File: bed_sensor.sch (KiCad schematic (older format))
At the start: 22 parts, among them J1 Conn_01x02, J4 Conn_01x02, J5 DM3AT-SF-PEJM5, Q1 2N2219, SW1 SW_SPST, U1 MIC5205-3.3, U2 MPU-9250, U5 CFAH0802D-YYH-JP

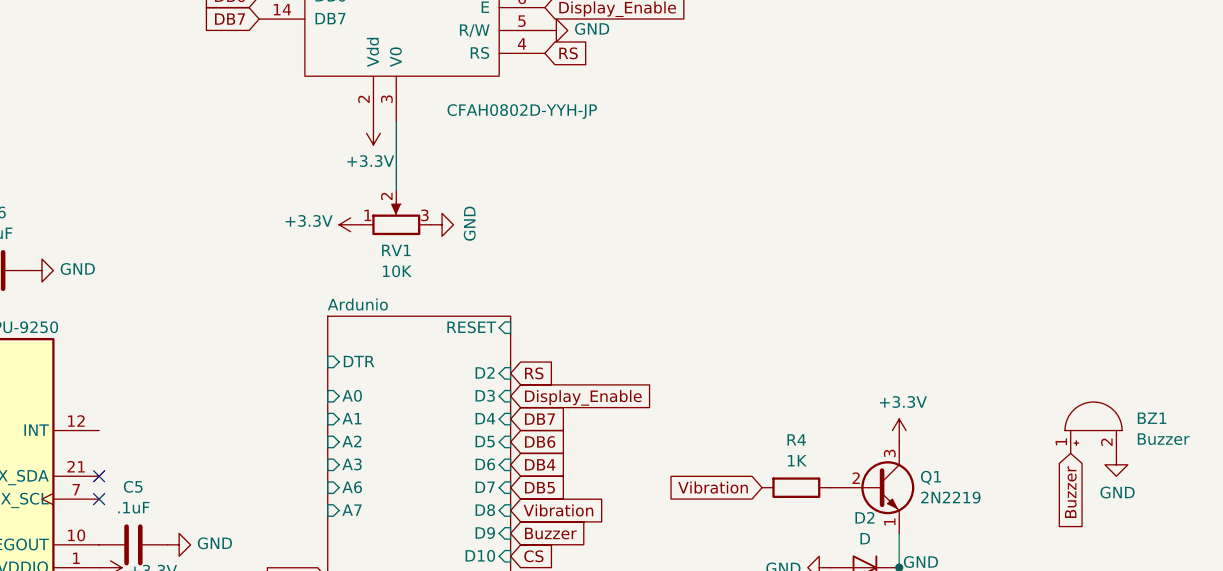
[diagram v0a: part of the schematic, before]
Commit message: added toggle button to side of board
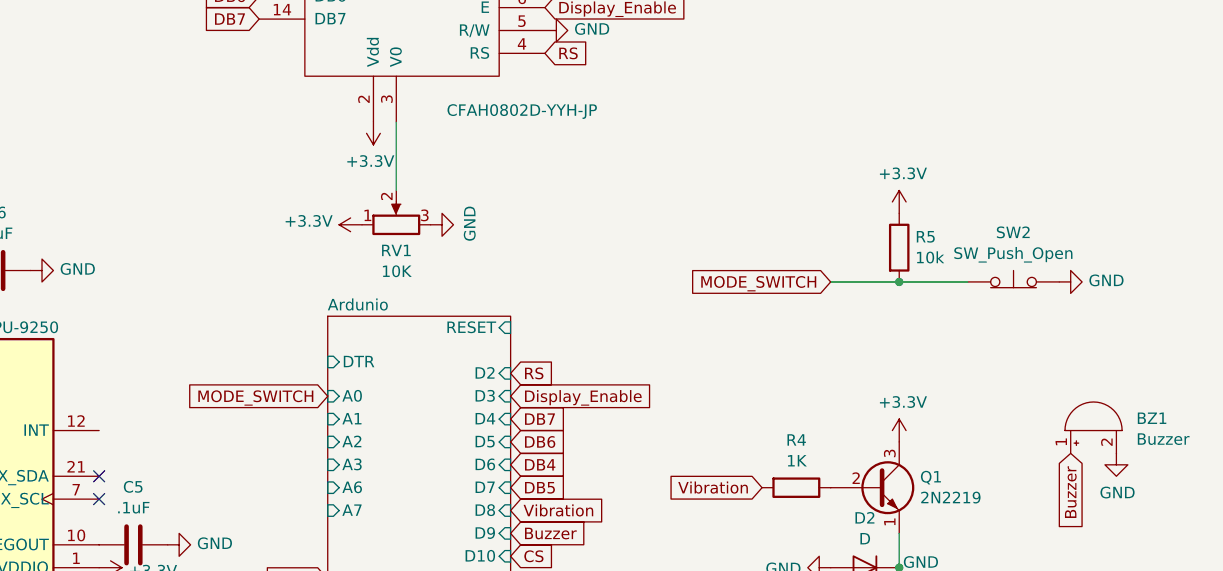
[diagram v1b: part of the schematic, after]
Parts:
- added R5: 10k, Resistor_SMD:R_0805_2012Metric, symbol Device:R
- added SW2: SW_Push_Open, Button_Switch_THT:SW_Tactile_SKHH_Angled, symbol Switch:SW_Push_Open
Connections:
- net +3V3: now also R5.1
- net GND: now also SW2.2 (B)
- new net MODE_SWITCH: R5.2, SW2.1 (A)
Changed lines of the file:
@@
 SCK
 $Comp
-L power:GND #PWR?
+L power:GND #PWR0117
 U 1 1 5B293C50
 P 4350 7200
-F 0 "#PWR?" H 4350 6950 50  0001 C CNN
+F 0 "#PWR0117" H 4350 6950 50  0001 C CNN
 F 1 "GND" V 4355 7072 50  0000 R CNN
 F 2 "" H 4350 7200 50  0001 C CNN
@@
 Text GLabel 4350 6600 0    50   Input ~ 0
 MISO
+$Comp
+L power:+3.3V #PWR0120
+U 1 1 5B2D3738
+P 7050 3800
+F 0 "#PWR0120" H 7050 3650 50  0001 C CNN
+F 1 "+3.3V" H 7065 3973 50  0000 C CNN
+F 2 "" H 7050 3800 50  0001 C CNN
+F 3 "" H 7050 3800 50  0001 C CNN
+	1    7050 3800
+	1    0    0    -1
+$EndComp
+$Comp
+L Device:R R5
+U 1 1 5B2D37B1
+P 7050 3950
+F 0 "R5" H 7120 3996 50  0000 L CNN
+F 1 "10k" H 7120 3905 50  0000 L CNN
+F 2 "Resistor_SMD:R_0805_2012Metric" V 6980 3950 50  0001 C CNN
+F 3 "~" H 7050 3950 50  0001 C CNN
+	1    7050 3950
+	1    0    0    -1
+$EndComp
+Text GLabel 4550 4600 0    50   Input ~ 0
+MODE_SWITCH
+Text GLabel 6750 4100 0    50   Input ~ 0
+MODE_SWITCH
+Wire Wire Line
+	6750 4100 7050 4100
+Wire Wire Line
+	7050 4100 7350 4100
+Connection ~ 7050 4100
+$Comp
+L Switch:SW_Push_Open SW2
+U 1 1 5B2D57E5
+P 7550 4100
+F 0 "SW2" H 7550 4315 50  0000 C CNN
+F 1 "SW_Push_Open" H 7550 4224 50  0000 C CNN
+F 2 "Button_Switch_THT:SW_Tactile_SKHH_Angled" H 7550 4300 50  0001 C CNN
+F 3 "" H 7550 4300 50  0001 C CNN
+	1    7550 4100
+	1    0    0    -1
+$EndComp
+$Comp
+L power:GND #PWR0121
+U 1 1 5B2D5928
+P 7750 4100
+F 0 "#PWR0121" H 7750 3850 50  0001 C CNN
+F 1 "GND" V 7755 3972 50  0000 R CNN
+F 2 "" H 7750 4100 50  0001 C CNN
+F 3 "" H 7750 4100 50  0001 C CNN
+	1    7750 4100
+	0    -1   -1   0
+$EndComp
 $EndSCHEMATC

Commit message: flipped screen
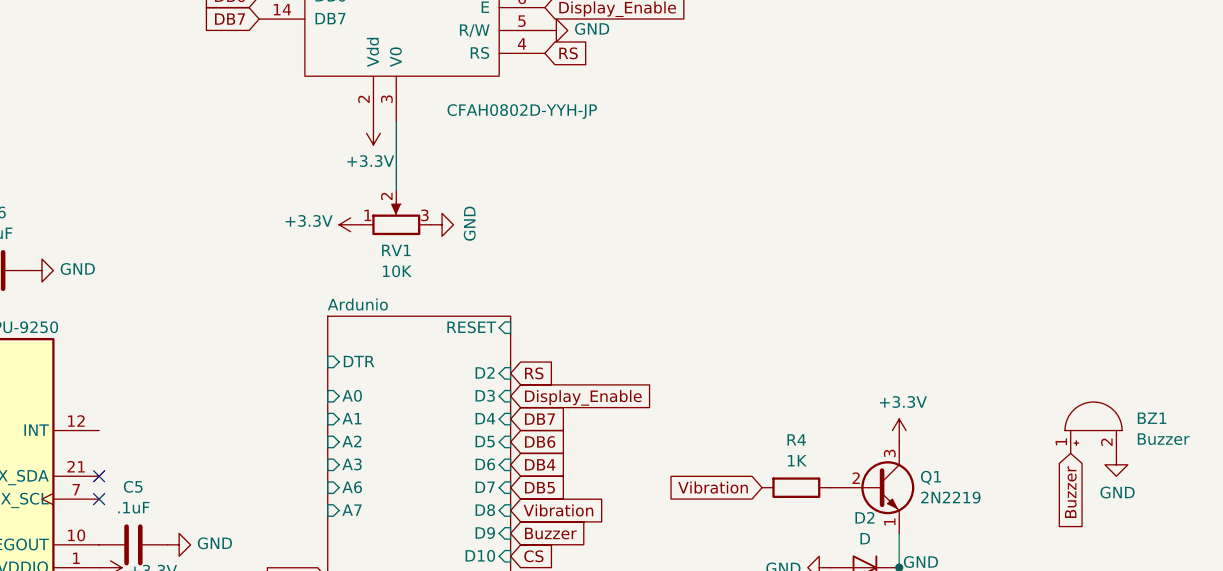
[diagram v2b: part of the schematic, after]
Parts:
- removed R5: 10k, Resistor_SMD:R_0805_2012Metric, symbol Device:R
- removed SW2: SW_Push_Open, Button_Switch_THT:SW_Tactile_SKHH_Angled, symbol Switch:SW_Push_Open
- RV1: footprint Potentiometers:Potentiometer_Trimmer_ACP_CA9h2.5_Vertical_Px2.5mm_Py5.0mm -> components:BI P090L-02F25BR10K
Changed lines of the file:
@@
 F 0 "RV1" V 4736 3850 50  0000 C CNN
 F 1 "10K" V 4645 3850 50  0000 C CNN
-F 2 "Potentiometers:Potentiometer_Trimmer_ACP_CA9h2.5_Vertical_Px2.5mm_Py5.0mm" H 4850 3850 50  0001 C CNN
+F 2 "components:BI P090L-02F25BR10K" H 4850 3850 50  0001 C CNN
 F 3 "~" H 4850 3850 50  0001 C CNN
 	1    4850 3850
@@
 Text GLabel 4350 6600 0    50   Input ~ 0
 MISO
-$Comp
-L power:+3.3V #PWR0120
-U 1 1 5B2D3738
-P 7050 3800
-F 0 "#PWR0120" H 7050 3650 50  0001 C CNN
-F 1 "+3.3V" H 7065 3973 50  0000 C CNN
-F 2 "" H 7050 3800 50  0001 C CNN
-F 3 "" H 7050 3800 50  0001 C CNN
-	1    7050 3800
-	1    0    0    -1
-$EndComp
-$Comp
-L Device:R R5
-U 1 1 5B2D37B1
-P 7050 3950
-F 0 "R5" H 7120 3996 50  0000 L CNN
-F 1 "10k" H 7120 3905 50  0000 L CNN
-F 2 "Resistor_SMD:R_0805_2012Metric" V 6980 3950 50  0001 C CNN
-F 3 "~" H 7050 3950 50  0001 C CNN
-	1    7050 3950
-	1    0    0    -1
-$EndComp
-Text GLabel 4550 4600 0    50   Input ~ 0
-MODE_SWITCH
-Text GLabel 6750 4100 0    50   Input ~ 0
-MODE_SWITCH
-Wire Wire Line
-	6750 4100 7050 4100
-Wire Wire Line
-	7050 4100 7350 4100
-Connection ~ 7050 4100
-$Comp
-L Switch:SW_Push_Open SW2
-U 1 1 5B2D57E5
-P 7550 4100
-F 0 "SW2" H 7550 4315 50  0000 C CNN
-F 1 "SW_Push_Open" H 7550 4224 50  0000 C CNN
-F 2 "Button_Switch_THT:SW_Tactile_SKHH_Angled" H 7550 4300 50  0001 C CNN
-F 3 "" H 7550 4300 50  0001 C CNN
-	1    7550 4100
-	1    0    0    -1
-$EndComp
-$Comp
-L power:GND #PWR0121
-U 1 1 5B2D5928
-P 7750 4100
-F 0 "#PWR0121" H 7750 3850 50  0001 C CNN
-F 1 "GND" V 7755 3972 50  0000 R CNN
-F 2 "" H 7750 4100 50  0001 C CNN
-F 3 "" H 7750 4100 50  0001 C CNN
-	1    7750 4100
-	0    -1   -1   0
-$EndComp
 $EndSCHEMATC

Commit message: updated layout for thumb pot
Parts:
- RV1: footprint components:BI P090L-02F25BR10K -> Connector_PinSocket_2.54mm:PinSocket_1x03_P2.54mm_Vertical
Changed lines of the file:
@@
 F 0 "RV1" V 4736 3850 50  0000 C CNN
 F 1 "10K" V 4645 3850 50  0000 C CNN
-F 2 "components:BI P090L-02F25BR10K" H 4850 3850 50  0001 C CNN
+F 2 "Connector_PinSocket_2.54mm:PinSocket_1x03_P2.54mm_Vertical" H 4850 3850 50  0001 C CNN
 F 3 "~" H 4850 3850 50  0001 C CNN
 	1    4850 3850
